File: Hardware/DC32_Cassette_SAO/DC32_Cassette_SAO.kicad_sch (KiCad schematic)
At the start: 17 parts, among them J1 Conn_02x03_Top_Bottom

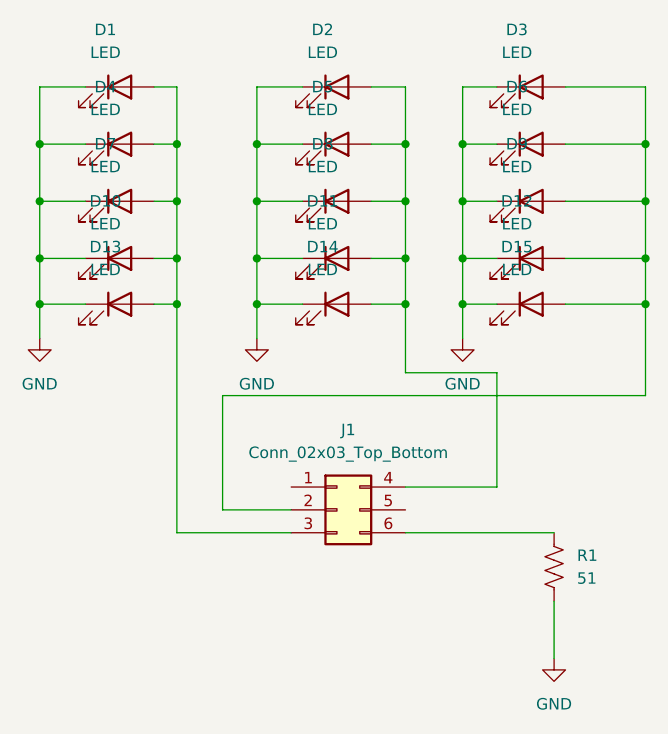
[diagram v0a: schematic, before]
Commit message: Updated schematics and generated PDFs
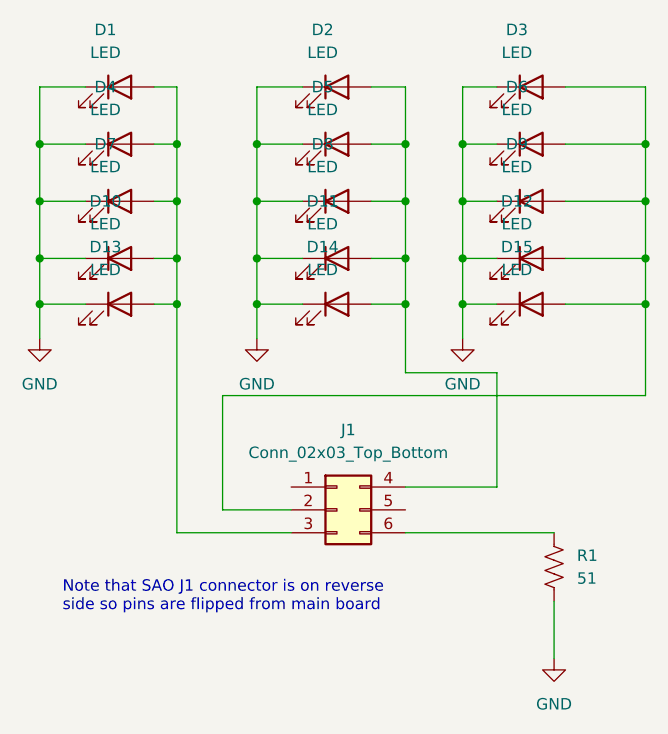
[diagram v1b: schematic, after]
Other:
- note added: "Note that SAO J1 connector is on reverse side so pins are flipped from main board"
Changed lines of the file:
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@@
     (stroke (width 0) (type default))
+  )
+  (text "Note that SAO J1 connector is on reverse\nside so pins are flipped from main board"
+    (at 107.95 105.41 0)
+    (effects (font (size 1.27 1.27)) (justify left bottom))
   )
   (symbol (lib_id "Device:LED") (at 160.02 59.69 0) (unit 1)
